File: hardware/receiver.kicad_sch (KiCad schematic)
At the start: 28 parts, among them J1 USB-C, J2 Left, J3 Right, U1 AMS1117-3.3, U2 AMS1117-3.3, U3 AMS1117-3.3, U4 ESP32-WROOM-32E, U5 PCM5102A

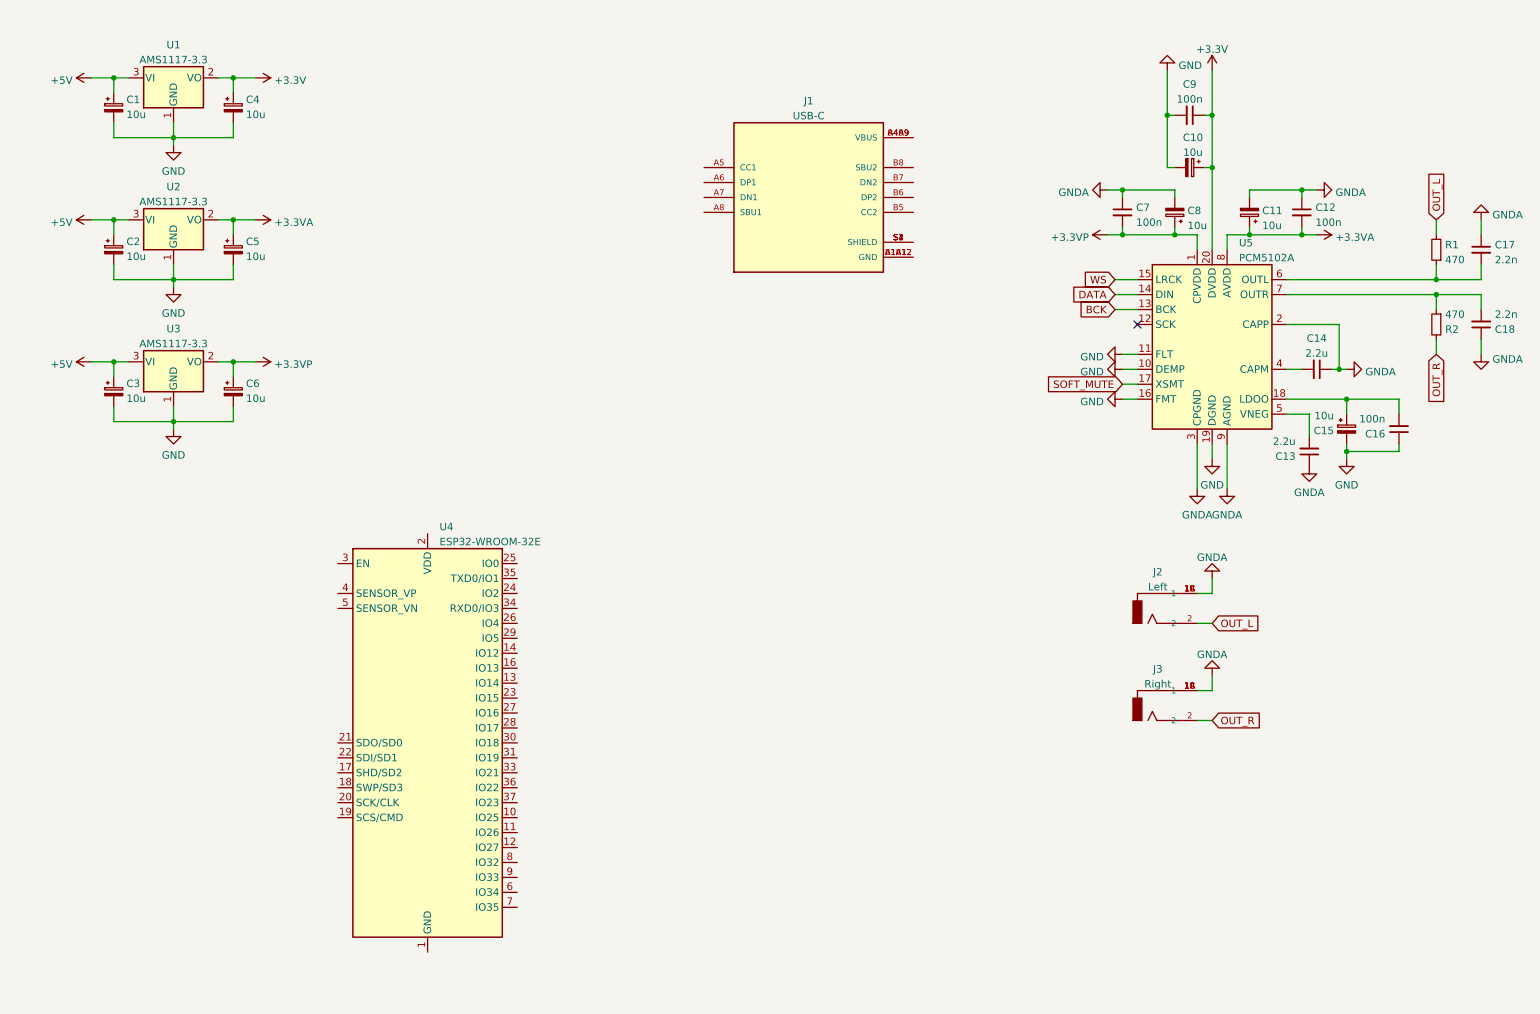
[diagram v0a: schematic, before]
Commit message: Worked on schematic and split parts into seperate schematics
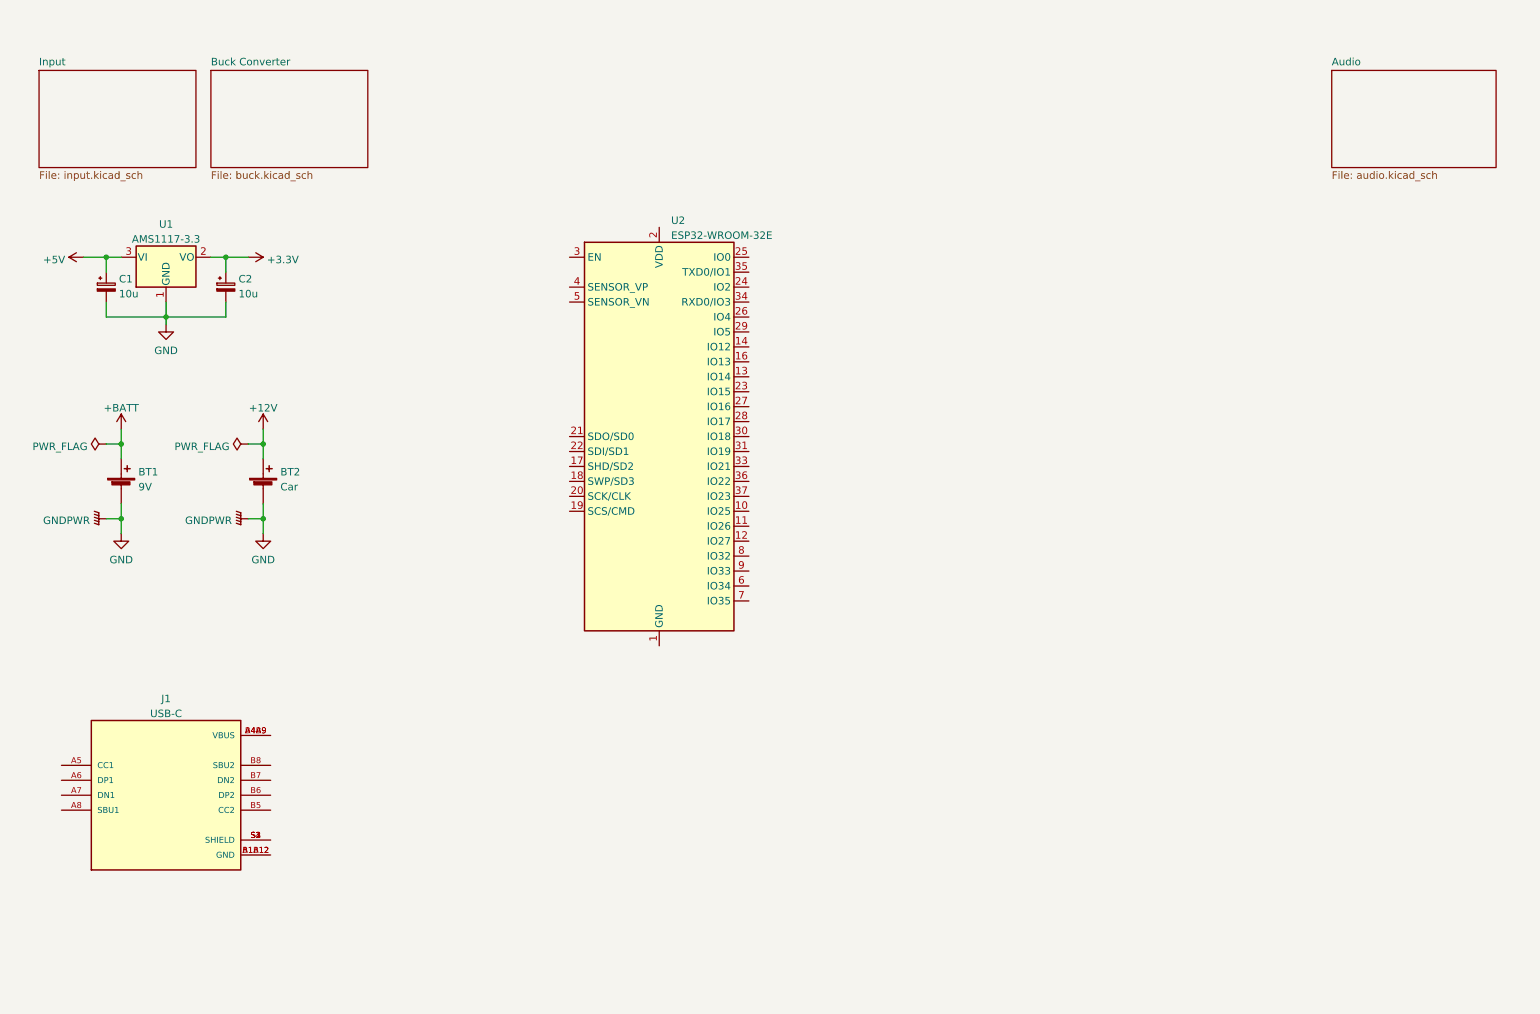
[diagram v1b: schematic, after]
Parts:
- removed C10, C11, C15, C2, C3, C5, C6, C8: 10u, Capacitor_SMD:C_1206_3216Metric, symbol Device:C_Polarized_Small
- removed C12, C16, C7, C9: 100n, Capacitor_SMD:C_0402_1005Metric, symbol Device:C_Small
- removed C13, C14: 2.2u, Capacitor_SMD:C_0402_1005Metric, symbol Device:C_Small
- removed C17, C18: 2.2n, Capacitor_SMD:C_0805_2012Metric, symbol Device:C_Small
- removed J2: Left, RCJ-013:CUI_RCJ-013, symbol RCJ-013:RCJ-013
- removed J3: Right, RCJ-013:CUI_RCJ-013, symbol RCJ-013:RCJ-013
- removed R1, R2: 470, Resistor_SMD:R_0402_1005Metric, symbol Device:R_Small
- removed U2, U3: AMS1117-3.3, Package_TO_SOT_SMD:SOT-223-3_TabPin2, symbol Regulator_Linear:AMS1117-3.3
- removed U5: PCM5102A, Package_SO:TSSOP-20_4.4x6.5mm_P0.65mm, symbol Audio:PCM5102
- added BT1: 9V, TestPoint:TestPoint_2Pads_Pitch2.54mm_Drill0.8mm, symbol Device:Battery_Cell
- added BT2: Car, TestPoint:TestPoint_2Pads_Pitch2.54mm_Drill0.8mm, symbol Device:Battery_Cell
- U2: renamed from U4; LCSC# (none) -> C701341; LSCS# C701341 -> (none)
- renumbered C4 to C2
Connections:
- net GND: now also BT1.2 (-), BT2.2 (-)
- new net +12V: BT2.1 (+)
- new net +BATT: BT1.1 (+)
- no-connect marks 1 -> 0
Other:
- added sheet Audio (audio.kicad_sch)
- added sheet Buck Converter (buck.kicad_sch)
- added sheet Input (input.kicad_sch)
- moved on the sheet: C1, C2, J1, U1, U2

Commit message: Finished first iteration of the PCB
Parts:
- removed BT1: 9V, TestPoint:TestPoint_2Pads_Pitch2.54mm_Drill0.8mm, symbol Device:Battery_Cell
- removed BT2: Car, TestPoint:TestPoint_2Pads_Pitch2.54mm_Drill0.8mm, symbol Device:Battery_Cell
- added C1, C26, C27, C28, C4, C5: 100n, Capacitor_SMD:C_0402_1005Metric, symbol Device:C_Small
- added D1: Green, LED_SMD:LED_0603_1608Metric, symbol Device:LED
- added D2: Blue, LED_SMD:LED_0603_1608Metric, symbol Device:LED
- added J1: Conn_01x05_Male, Connector_JST:JST_XH_S5B-XH-A-1_1x05_P2.50mm_Horizontal, symbol Connector:Conn_01x05_Male
- added J3: Left, RCJ-013:CUI_RCJ-013, symbol RCJ-013:RCJ-013
- added J4: Right, RCJ-013:CUI_RCJ-013, symbol RCJ-013:RCJ-013
- added Q1, Q2: S8050, Package_TO_SOT_SMD:SOT-23, symbol Transistor_BJT:S8050
- added R1, R4: 5.1k, Resistor_SMD:R_0402_1005Metric, symbol Device:R
- added R10, R11, R12, R2, R8: 10k, Resistor_SMD:R_0402_1005Metric, symbol Device:R
- added R3: 1M, Resistor_SMD:R_0402_1005Metric, symbol Device:R
- added R5, R6, R7, R9: 1k, Resistor_SMD:R_0402_1005Metric, symbol Device:R
- added SW1: Enable, Button_Switch_SMD:SW_SPST_SKQG_WithStem, symbol Switch:SW_Push
- added SW2: Boot, Button_Switch_SMD:SW_SPST_SKQG_WithStem, symbol Switch:SW_Push
- added TP1, TP11, TP19, TP8: GND, TestPoint:TestPoint_Pad_D1.0mm, symbol Connector:TestPoint
- added TP10: OUT_R, TestPoint:TestPoint_Pad_D1.0mm, symbol Connector:TestPoint
- added TP12: CAN_H, TestPoint:TestPoint_Pad_D1.0mm, symbol Connector:TestPoint
- added TP13: CAN_L, TestPoint:TestPoint_Pad_D1.0mm, symbol Connector:TestPoint
- added TP14: RX, TestPoint:TestPoint_Pad_D1.0mm, symbol Connector:TestPoint
- added TP15: TX, TestPoint:TestPoint_Pad_D1.0mm, symbol Connector:TestPoint
- added TP16: DTR, TestPoint:TestPoint_Pad_D1.0mm, symbol Connector:TestPoint
- added TP17: RTS, TestPoint:TestPoint_Pad_D1.0mm, symbol Connector:TestPoint
- added TP18, TP3: 5V, TestPoint:TestPoint_Pad_D1.0mm, symbol Connector:TestPoint
- added TP2: 3V3, TestPoint:TestPoint_Pad_D1.0mm, symbol Connector:TestPoint
- added TP4: V_in, TestPoint:TestPoint_Pad_D1.0mm, symbol Connector:TestPoint
- added TP5: CAR, TestPoint:TestPoint_Pad_D1.0mm, symbol Connector:TestPoint
- added TP6: DASH, TestPoint:TestPoint_Pad_D1.0mm, symbol Connector:TestPoint
- added TP7: SENSE, TestPoint:TestPoint_Pad_D1.0mm, symbol Connector:TestPoint
- added TP9: OUT_L, TestPoint:TestPoint_Pad_D1.0mm, symbol Connector:TestPoint
- added U1: SN65HVD230, Package_SO:SOIC-8_3.9x4.9mm_P1.27mm, symbol Interface_CAN_LIN:SN65HVD230
- added U2: CH340C, Package_SO:SOIC-16_3.9x9.9mm_P1.27mm, symbol Interface_USB:CH340C
- U3: renamed from U1; LCSC# (none) -> C6186; LSCS# C6186 -> (none)
- renumbered C1 to C2, C2 to C3, J1 to J2, U2 to U4
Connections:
- net +3V3: now also U4.2 (VDD), C1.2, C26.1, C27.1, C28.1, R11.2, R12.2, R7.1, TP2.1, U1.3 (VCC), U2.16 (VCC), U2.4 (V3)
- net +5V: now also J2.A4B9 (VBUS), J2.B4A9 (VBUS), TP18.1, TP3.1
- net GND: now also J2.A1B12 (GND), J2.B1A12 (GND), U4.1 (GND), U4.15 (GND), U4.38 (GND), U4.39 (GND), C1.1, C26.2, C27.2, C28.2, C4.2, C5.2, D1.1 (K), D2.1 (K), J1.5 (Pin_5), J3.1A (1), J3.1B (1), J3.1C (1), J4.1A (1), J4.1B (1), J4.1C (1), R1.1, R3.2, R4.2, SW1.1, SW2.1, TP1.1, TP11.1, TP19.1, TP8.1, U1.2 (GND), U2.1 (GND)
- net at J2.A5 (CC1): now also R1.2
- net D+: now reaches J2.A6 (DP1)
- net D+: now also J2.B6 (DP2), U2.5 (UD+)
- net D-: now reaches J2.A7 (DN1)
- net D-: now also J2.B7 (DN2), U2.6 (UD-)
- net at J2.B5 (CC2): now also R4.1
- net at J2.S1 (SHIELD), J2.S2 (SHIELD), J2.S3 (SHIELD)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: now also R3.1
- net Sense: now reaches U4.10 (IO25)
- net Sense: now also TP7.1
- net BOOT: now reaches U4.25 (IO0)
- net BOOT: now also C5.1, Q1.3 (C), R12.1, SW2.2
- net MUTE: now reaches U4.26 (IO4)
- net WS: now reaches U4.27 (IO16)
- net DATA: now reaches U4.28 (IO17)
- net BCK: now reaches U4.29 (IO5)
- net EN: now reaches U4.3 (EN)
- net EN: now also C4.1, Q2.3 (C), R11.1, SW1.2
- net RX: now reaches U4.34 (RXD0/IO3)
- net RX: now also R5.1, TP14.1
- net TX: now reaches U4.35 (TXD0/IO1)
- net TX: now also R6.1, TP15.1
- net BLUE: now reaches U4.6 (IO34)
- net BLUE: now also R9.1
- net CRX: now reaches U4.7 (IO35)
- net CRX: now also U1.4 (R)
- net CTX: now reaches U4.8 (IO32)
- net CTX: now also U1.1 (D)
- net MODE: now reaches U4.9 (IO33)
- net MODE: now also R2.1
- new net: D1.2 (A), R7.2
- new net: Q2.2 (B), R8.2
- new net: R5.2, U2.2 (TXD)
- new net: R2.2, U1.8 (Rs)
- new net: Q1.2 (B), R10.1
- new net: R6.2, U2.3 (RXD)
- new net: D2.2 (A), R9.2
- new net CAN+: J1.2 (Pin_2), TP12.1, U1.7 (CANH)
- new net CAN-: J1.3 (Pin_3), TP13.1, U1.6 (CANL)
- new net CAR: J1.4 (Pin_4), TP5.1
- new net DASH: J1.1 (Pin_1), TP6.1
- new net DTR: Q1.1 (E), R8.1, TP16.1, U2.13 (~{DTR})
- new net OUT_L: J3.2, TP9.1
- new net OUT_R: J4.2, TP10.1
- new net RTS: Q2.1 (E), R10.2, TP17.1, U2.14 (~{RTS})
- new net V_in: TP4.1
- no-connect marks 0 -> 14
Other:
- sheet Audio ports: added BCK, DATA, MUTE, OUT_L, OUT_R, WS; removed none
- sheet Buck Converter ports: added V_in; removed none
- sheet Input ports: added Car Battery, Dashboard Light, Sense, V_in; removed none
- note added: "NOT BROKEN OUT!"
- moved on the sheet: C2, C3, J2, U3, U4

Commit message: Made corners rounded and added mounting holes
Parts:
- added H1, H2, H3, H4: M2, MountingHole:MountingHole_2.2mm_M2_ISO14580_Pad, symbol Mechanical:MountingHole_Pad
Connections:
- net GND: now also H1.1, H2.1, H3.1, H4.1
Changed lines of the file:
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@@
+    (stroke (width 0) (type default) (color 0 0 0 0))
+  )
+  (wire (pts (xy 154.94 168.91) (xy 154.94 172.72))
     (stroke (width 0) (type default) (color 0 0 0 0))
   )
@@
     (stroke (width 0) (type default) (color 0 0 0 0))
   )
+  (wire (pts (xy 163.83 168.91) (xy 163.83 172.72))
+    (stroke (width 0) (type default) (color 0 0 0 0))
+  )
   (wire (pts (xy 236.22 81.28) (xy 242.57 81.28))
     (stroke (width 0) (type default) (color 0 0 0 0))
@@
     (stroke (width 0) (type default) (color 0 0 0 0))
   )
+  (wire (pts (xy 137.16 168.91) (xy 137.16 172.72))
+    (stroke (width 0) (type default) (color 0 0 0 0))
+  )
   (wire (pts (xy 93.98 132.715) (xy 93.98 135.255))
     (stroke (width 0) (type default) (color 0 0 0 0))
@@
     (stroke (width 0) (type default) (color 0 0 0 0))
   )
+  (wire (pts (xy 146.05 168.91) (xy 146.05 172.72))
+    (stroke (width 0) (type default) (color 0 0 0 0))
+  )
   (wire (pts (xy 140.335 116.84) (xy 143.51 116.84))
     (stroke (width 0) (type default) (color 0 0 0 0))
@@
   (label "TX" (at 143.51 124.46 180)
     (effects (font (size 1.27 1.27)) (justify right bottom))
+  )
+  (symbol (lib_id "Mechanical:MountingHole_Pad") (at 163.83 166.37 0) (unit 1)
+    (in_bom yes) (on_board yes)
+    (property "Reference" "H4" (id 0) (at 169.3078 165.1 90))
+    (property "Value" "M2" (id 1) (at 166.7709 165.1 90))
+    (property "Footprint" "MountingHole:MountingHole_2.2mm_M2_ISO14580_Pad" (id 2) (at 163.83 166.37 0)
+      (effects (font (size 1.27 1.27)) hide)
+    )
+    (property "Datasheet" "~" (id 3) (at 163.83 166.37 0)
+      (effects (font (size 1.27 1.27)) hide)
+    )
+    (pin "1")
   )
   (symbol (lib_id "Device:LED") (at 168.91 38.735 90) (unit 1)
@@
     (pin "1")
     (pin "2")
+  )
+  (symbol (lib_id "power:GND") (at 163.83 172.72 0) (unit 1)
+    (in_bom yes) (on_board yes) (fields_autoplaced)
+    (property "Reference" "#PWR0107" (id 0) (at 163.83 179.07 0)
+      (effects (font (size 1.27 1.27)) hide)
+    )
+    (property "Value" "GND" (id 1) (at 163.3962 175.895 90)
+      (effects (font (size 1.27 1.27)) (justify right))
+    )
+    (property "Footprint" "" (id 2) (at 163.83 172.72 0)
+      (effects (font (size 1.27 1.27)) hide)
+    )
+    (property "Datasheet" "" (id 3) (at 163.83 172.72 0)
+      (effects (font (size 1.27 1.27)) hide)
+    )
+    (pin "1")
   )
   (symbol (lib_id "power:GND") (at 93.98 135.255 0) (unit 1)
@@
     (pin "1")
     (pin "2")
+  )
+  (symbol (lib_id "power:GND") (at 146.05 172.72 0) (unit 1)
+    (in_bom yes) (on_board yes) (fields_autoplaced)
+    (property "Reference" "#PWR0105" (id 0) (at 146.05 179.07 0)
+      (effects (font (size 1.27 1.27)) hide)
+    )
+    (property "Value" "GND" (id 1) (at 145.6162 175.895 90)
+      (effects (font (size 1.27 1.27)) (justify right))
+    )
+    (property "Footprint" "" (id 2) (at 146.05 172.72 0)
+      (effects (font (size 1.27 1.27)) hide)
+    )
+    (property "Datasheet" "" (id 3) (at 146.05 172.72 0)
+      (effects (font (size 1.27 1.27)) hide)
+    )
+    (pin "1")
   )
   (symbol (lib_id "Device:C_Small") (at 224.155 136.525 0) (unit 1)
@@
     (pin "1")
   )
+  (symbol (lib_id "power:GND") (at 137.16 172.72 0) (unit 1)
+    (in_bom yes) (on_board yes) (fields_autoplaced)
+    (property "Reference" "#PWR0104" (id 0) (at 137.16 179.07 0)
+      (effects (font (size 1.27 1.27)) hide)
+    )
+    (property "Value" "GND" (id 1) (at 136.7262 175.895 90)
+      (effects (font (size 1.27 1.27)) (justify right))
+    )
+    (property "Footprint" "" (id 2) (at 137.16 172.72 0)
+      (effects (font (size 1.27 1.27)) hide)
+    )
+    (property "Datasheet" "" (id 3) (at 137.16 172.72 0)
+      (effects (font (size 1.27 1.27)) hide)
+    )
+    (pin "1")
+  )
   (symbol (lib_id "Device:C_Small") (at 113.03 109.22 90) (unit 1)
     (in_bom yes) (on_board yes) (fields_autoplaced)
@@
     (pin "1")
   )
+  (symbol (lib_id "Mechanical:MountingHole_Pad") (at 146.05 166.37 0) (unit 1)
+    (in_bom yes) (on_board yes)
+    (property "Reference" "H2" (id 0) (at 151.5278 165.1 90))
+    (property "Value" "M2" (id 1) (at 148.9909 165.1 90))
+    (property "Footprint" "MountingHole:MountingHole_2.2mm_M2_ISO14580_Pad" (id 2) (at 146.05 166.37 0)
+      (effects (font (size 1.27 1.27)) hide)
+    )
+    (property "Datasheet" "~" (id 3) (at 146.05 166.37 0)
+      (effects (font (size 1.27 1.27)) hide)
+    )
+    (pin "1")
+  )
   (symbol (lib_id "Device:R") (at 179.07 135.89 90) (unit 1)
     (in_bom yes) (on_board yes) (fields_autoplaced)
@@
     (pin "1")
     (pin "2")
+  )
+  (symbol (lib_id "power:GND") (at 154.94 172.72 0) (unit 1)
+    (in_bom yes) (on_board yes) (fields_autoplaced)
+    (property "Reference" "#PWR0106" (id 0) (at 154.94 179.07 0)
+      (effects (font (size 1.27 1.27)) hide)
+    )
+    (property "Value" "GND" (id 1) (at 154.5062 175.895 90)
+      (effects (font (size 1.27 1.27)) (justify right))
+    )
+    (property "Footprint" "" (id 2) (at 154.94 172.72 0)
+      (effects (font (size 1.27 1.27)) hide)
+    )
+    (property "Datasheet" "" (id 3) (at 154.94 172.72 0)
+      (effects (font (size 1.27 1.27)) hide)
+    )
+    (pin "1")
   )
   (symbol (lib_id "power:+3V3") (at 243.205 116.205 0) (unit 1)
@@
     )
     (property "Datasheet" "~" (id 3) (at 76.835 168.275 0)
+      (effects (font (size 1.27 1.27)) hide)
+    )
+    (pin "1")
+  )
+  (symbol (lib_id "Mechanical:MountingHole_Pad") (at 137.16 166.37 0) (unit 1)
+    (in_bom yes) (on_board yes)
+    (property "Reference" "H1" (id 0) (at 142.6378 165.1 90))
+    (property "Value" "M2" (id 1) (at 140.1009 165.1 90))
+    (property "Footprint" "MountingHole:MountingHole_2.2mm_M2_ISO14580_Pad" (id 2) (at 137.16 166.37 0)
+      (effects (font (size 1.27 1.27)) hide)
+    )
+    (property "Datasheet" "~" (id 3) (at 137.16 166.37 0)
       (effects (font (size 1.27 1.27)) hide)
     )
@@
     (pin "1")
   )
+  (symbol (lib_id "Mechanical:MountingHole_Pad") (at 154.94 166.37 0) (unit 1)
+    (in_bom yes) (on_board yes)
+    (property "Reference" "H3" (id 0) (at 160.4178 165.1 90))
+    (property "Value" "M2" (id 1) (at 157.8809 165.1 90))
+    (property "Footprint" "MountingHole:MountingHole_2.2mm_M2_ISO14580_Pad" (id 2) (at 154.94 166.37 0)
+      (effects (font (size 1.27 1.27)) hide)
+    )
+    (property "Datasheet" "~" (id 3) (at 154.94 166.37 0)
+      (effects (font (size 1.27 1.27)) hide)
+    )
+    (pin "1")
+  )
   (symbol (lib_id "Device:R") (at 178.435 28.575 0) (unit 1)
     (in_bom yes) (on_board yes) (fields_autoplaced)
@@
       (reference "#PWR0103") (unit 1) (value "GND") (footprint "")
     )
+    (path "/8c2eec30-cbc2-4231-86c7-3ccccd8bc799"
+      (reference "#PWR0104") (unit 1) (value "GND") (footprint "")
+    )
+    (path "/63f47c92-0752-40f2-b0bf-64c23dbc3929"
+      (reference "#PWR0105") (unit 1) (value "GND") (footprint "")
+    )
+    (path "/bdcf5409-d4a0-4429-9fd5-e71cb40c974f"
+      (reference "#PWR0106") (unit 1) (value "GND") (footprint "")
+    )
+    (path "/433b3b44-1996-4089-8ad8-2ea0075dd80b"
+      (reference "#PWR0107") (unit 1) (value "GND") (footprint "")
+    )
     (path "/94475fec-2da2-4ee8-9e2a-f99d827b500e"
       (reference "C1") (unit 1) (value "100n") (footprint "Capacitor_SMD:C_0402_1005Metric")
@@
       (reference "D4") (unit 1) (value "1N5819WS") (footprint "Diode_SMD:D_SOD-323")
     )
+    (path "/d3065072-8983-4d93-89e3-2335903fadb5"
+      (reference "H1") (unit 1) (value "M2") (footprint "MountingHole:MountingHole_2.2mm_M2_ISO14580_Pad")
+    )
+    (path "/ba810a87-da8d-44d9-b337-13672f78aad4"
+      (reference "H2") (unit 1) (value "M2") (footprint "MountingHole:MountingHole_2.2mm_M2_ISO14580_Pad")
+    )
+    (path "/efb7a433-244a-45a9-a26e-efb92dd653c9"
+      (reference "H3") (unit 1) (value "M2") (footprint "MountingHole:MountingHole_2.2mm_M2_ISO14580_Pad")
+    )
+    (path "/04190376-a94b-458e-a715-71ffaad34dc8"
+      (reference "H4") (unit 1) (value "M2") (footprint "MountingHole:MountingHole_2.2mm_M2_ISO14580_Pad")
+    )
     (path "/b1d506a8-b29c-43b0-b851-d720e84b2408"

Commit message: Updated to new version of KiCad and made some small changes to the design
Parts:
- added D4: 1N5819WS, Diode_SMD:D_SOD-323, symbol Device:D_Schottky
- TP18: value 5V -> VBUS
- U4: value ESP32-WROOM-32E -> ESP32-WROOM-32; LCSC# C701341 -> C95209
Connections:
- net +5V: now also D4.1 (K); no longer J2.A4B9 (VBUS), J2.B4A9 (VBUS), TP18.1
- net BLUE: now also U4.11 (IO26); no longer U4.6 (IO34)
- new net VBUS: D4.2 (A), J2.A4B9 (VBUS), J2.B4A9 (VBUS), TP18.1
